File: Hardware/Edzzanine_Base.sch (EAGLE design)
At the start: 6 parts

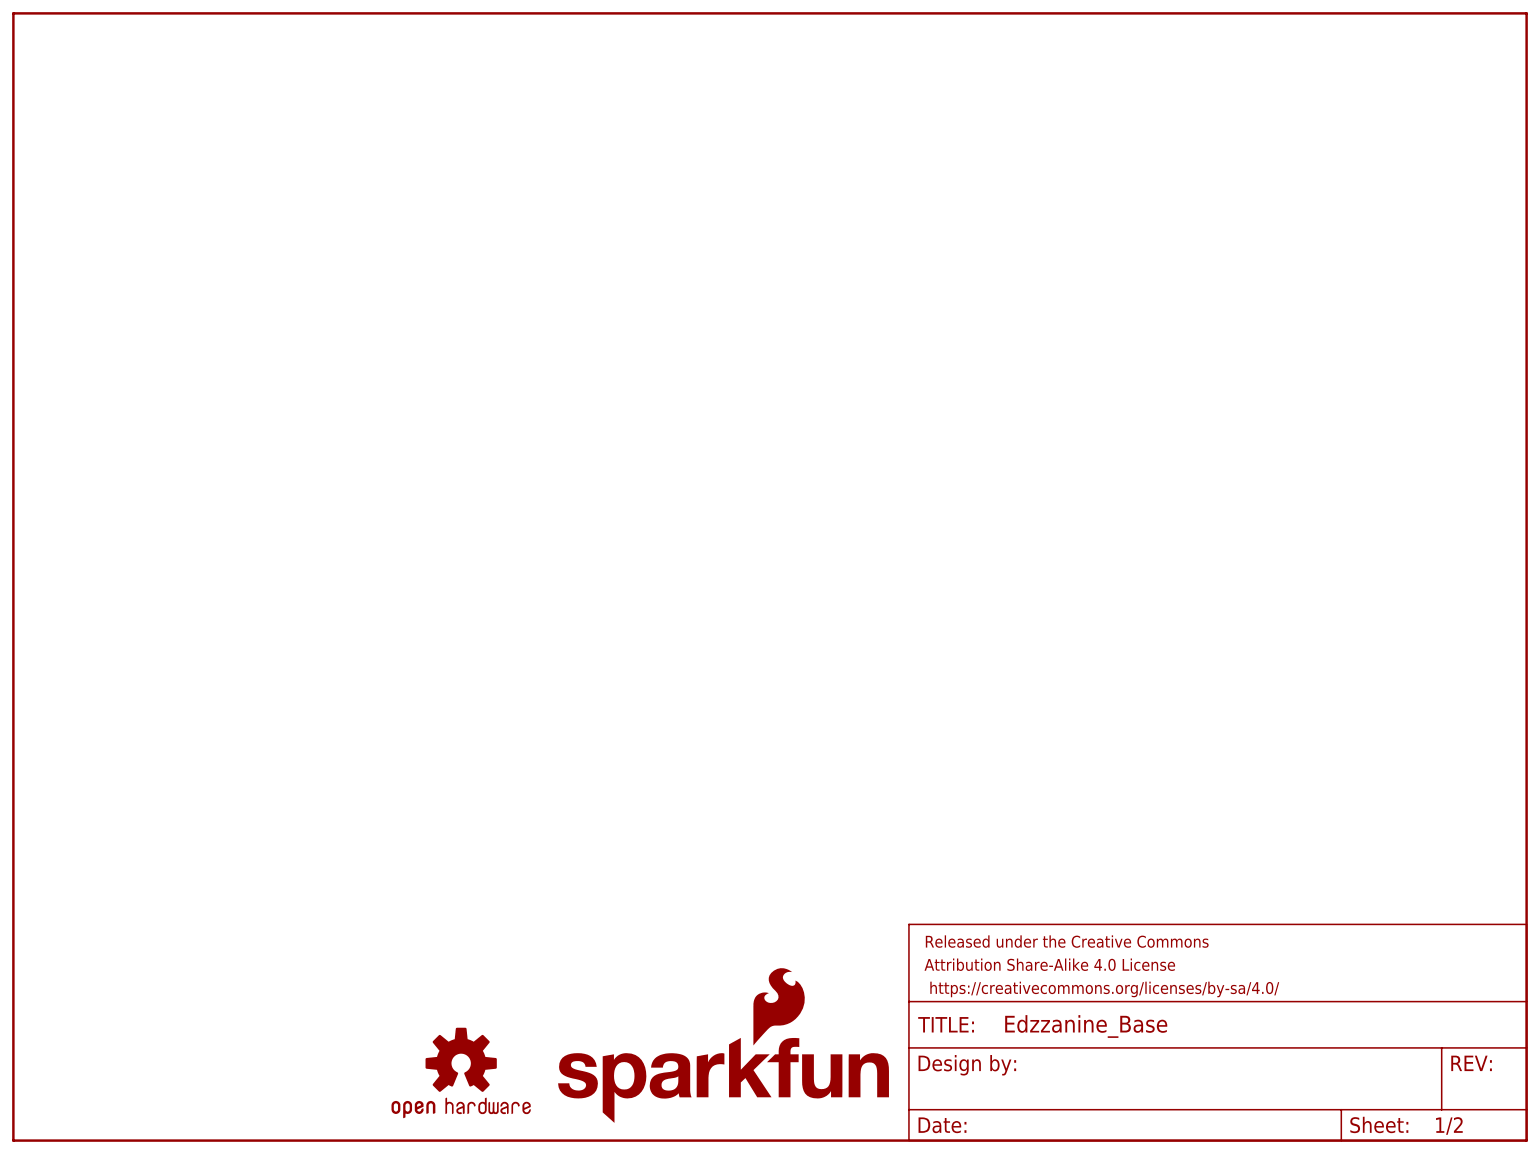
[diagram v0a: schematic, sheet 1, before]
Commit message: completed base layout, ready for review.  Removed testing layouts and other noise
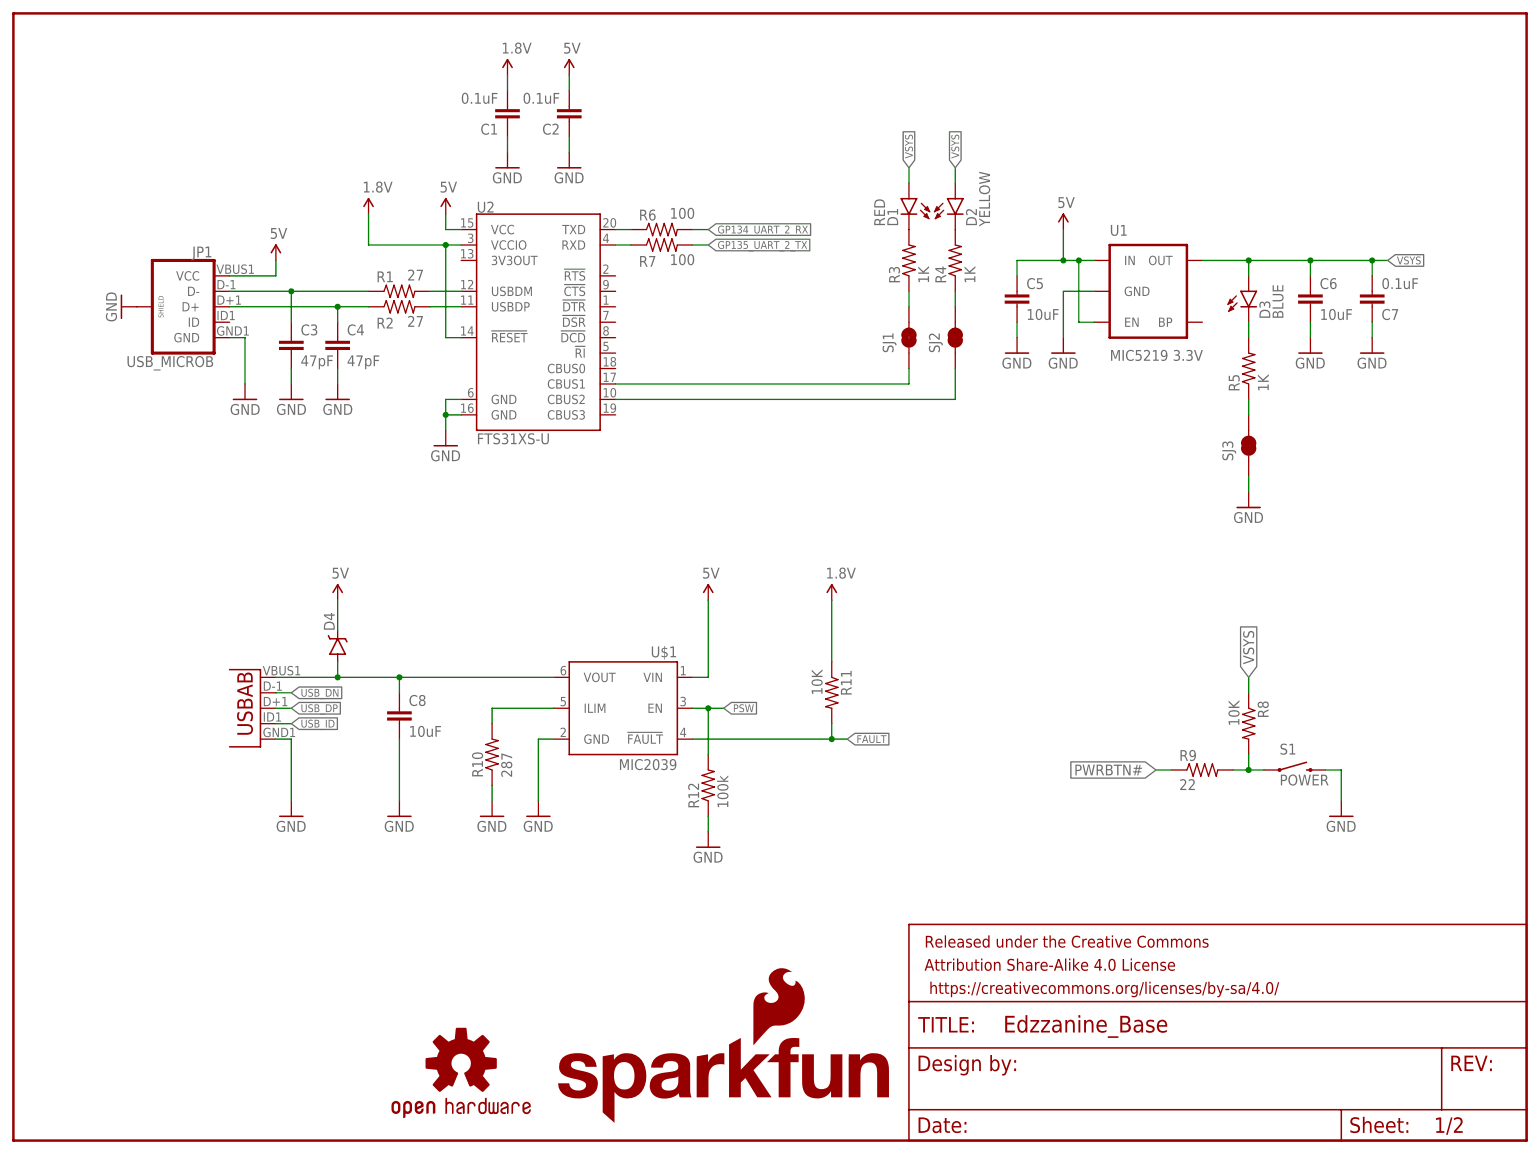
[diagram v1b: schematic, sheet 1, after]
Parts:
- added C1, C2, C7: 0.1uF, SparkFun-Capacitors:0.1UF-25V-5%(0603)
- added C3, C4: 47pF, SparkFun-Capacitors:47PF-50V-5%(0603)
- added C5, C6, C8: 10uF, SparkFun-Capacitors:10UF-6.3V-20%(1206)
- added D1: RED, SparkFun-LED:LED-RED0603
- added D2: YELLOW, SparkFun-LED:LED-YELLOW0603
- added D3: BLUE, SparkFun-LED:LED-BLUE0603
- added D4: DIODE-SCHOTTKY-MBRA140, SparkFun-DiscreteSemi:DIODE-SCHOTTKY-MBRA140
- added JP1: USB_MICROB, SparkFun-Connectors:USB_MICROB_PLUGCONN-11752
- added R1, R2: 27, SparkFun-Resistors:27OHM1/10W1%(0603)
- added R10: 287, SparkFun-Resistors:287OHM-1/10W-1%(0603)
- added R11, R8: 10K, SparkFun-Resistors:10KOHM1/10W1%(0603)0603
- added R12: 100k, SparkFun-Resistors:100KOHM1/10W1%(0603)
- added R3, R4, R5: 1K, SparkFun-Resistors:1KOHM1/10W1%(0603)
- added R6, R7: 100, SparkFun-Resistors:100OHM1/10W1%(0603)
- added R9: 22, SparkFun-Resistors:22OHM1/10W1%(0603)
- added S1: POWER, SparkFun-Electromechanical:SWITCH-MOMENTARY-2-SMD-1101NE
- added SJ1, SJ2, SJ3: JUMPER-PAD-2-NC_BY_TRACE, SparkFun-Passives:JUMPER-PAD-2-NC_BY_TRACE
- added U$1: MIC2039, Testing:MIC2039
- added U1: MIC5219 3.3V, SparkFun-PowerIC:V_REG_MIC52193.3V
- added U2: FTS31XS-U, SparkFun-DigitalIC:FT231XS
- added U3: (no value), SparkFun-Connectors:USB-ABCONN-11794
- renumbered U$2 to E1
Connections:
- new net 5V: C2.2, C5.1, D4.C, JP1.VCC, U$1.VIN, U1.EN, U1.IN, U2.VCC
- new net N$1: SJ1.1, U2.CBUS1
- new net N$10: D2.C, R4.2
- new net N$11: R6.1, U2.TXD
- new net N$12: D3.C, R5.2
- new net N$13: R5.1, SJ3.2
- new net N$14: R7.1, U2.RXD
- new net N$15: R8.2, R9.2, S1.1
- new net N$16: R10.2, U$1.ILIM
- new net N$18: C8.1, D4.A, U$1.VOUT, U3.VBUS
- new net N$2: C3.1, JP1.D-, R1.1
- new net N$3: C4.1, JP1.D+, R2.1
- new net N$4: R1.2, U2.USBDM
- new net N$5: R2.2, U2.USBDP
- new net N$6: SJ2.1, U2.CBUS2
- new net N$7: R3.1, SJ1.2
- new net N$8: R4.1, SJ2.2
- new net N$9: D1.C, R3.2
- net 1.8V: now also C1.2, R11.1, U2.!RESET, U2.VCCIO
- net FAULT: now also R11.2, U$1.!FAULT
- net GND: now also C1.1, C2.1, C3.2, C4.2, C5.2, C6.2, C7.1, C8.2, JP1.GND, JP1.SHIELD, R10.1, R12.1, S1.2, SJ3.1, U$1.GND, U1.GND, U2.GND@16, U2.GND@6, U3.GND
- net GP134_UART_2_RX: now also R6.2
- net GP135_UART_2_TX: now also R7.2
- net PSW: now also R12.2, U$1.EN
- net PWRBTN#: now also R9.1
- net USB_DN: now also U3.D-
- net USB_DP: now also U3.D+
- net USB_ID: now also U3.USBID
- net VSYS: now also C6.1, C7.2, D1.A, D2.A, D3.A, R8.1, U1.OUT
